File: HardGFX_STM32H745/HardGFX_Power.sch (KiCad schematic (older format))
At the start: 62 parts, among them J2 Conn_02x02_Odd_Even, J3 USB_C_Receptacle_USB2.0, U1 STM32H745BIT3, U2 ST1L05APU33R, U3 LD1117S18TR_SOT223, U4 LD1117S50TR_SOT223

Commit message: Add Info folder that contain data about reference design, datasheet component of references.
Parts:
- U1: value STM32H745BIT3 -> STM32H745BIT6; Digikey# (none) -> STM32H745BIT6-ND; MANUFACTURER (none) -> STMicroelectronics; Manf# (none) -> STM32H745BIT6
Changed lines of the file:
@@
 P 2650 1150
 F 0 "U1" H 3750 1537 60  0000 C CNN
-F 1 "STM32H745BIT3" H 3750 1431 60  0000 C CNN
+F 1 "STM32H745BIT6" H 3750 1431 60  0000 C CNN
 F 2 "STM32H745BIT3:STM32H745BIT3" H 3850 1390 60  0001 C CNN
 F 3 "https://www.st.com/resource/en/datasheet/stm32h745bi.pdf" H 2650 1150 60  0001 C CNN
+F 4 "STM32H745BIT6" H 2650 1150 50  0001 C CNN "Manf#"
+F 5 "STM32H745BIT6-ND" H 2650 1150 50  0001 C CNN "Digikey#"
+F 6 "STMicroelectronics" H 2650 1150 50  0001 C CNN "MANUFACTURER"
 	4    2650 1150
 	1    0    0    -1

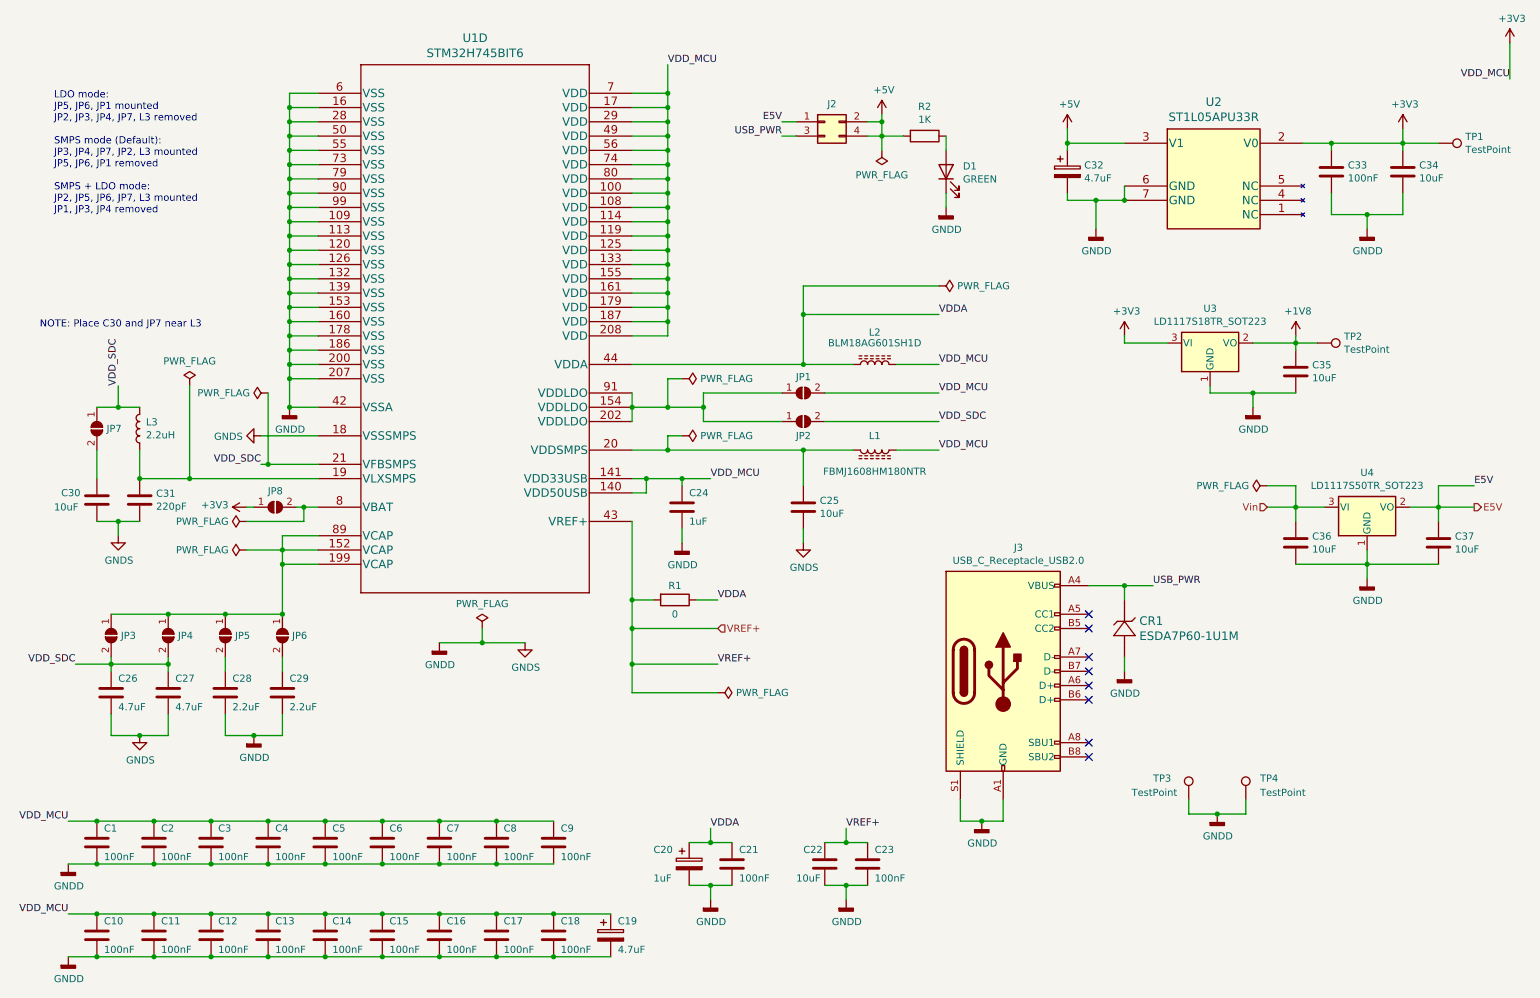
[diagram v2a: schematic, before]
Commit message: Filling field for do BOM with Kicost  and create proyect on IDE to start setting peripheral in MCU
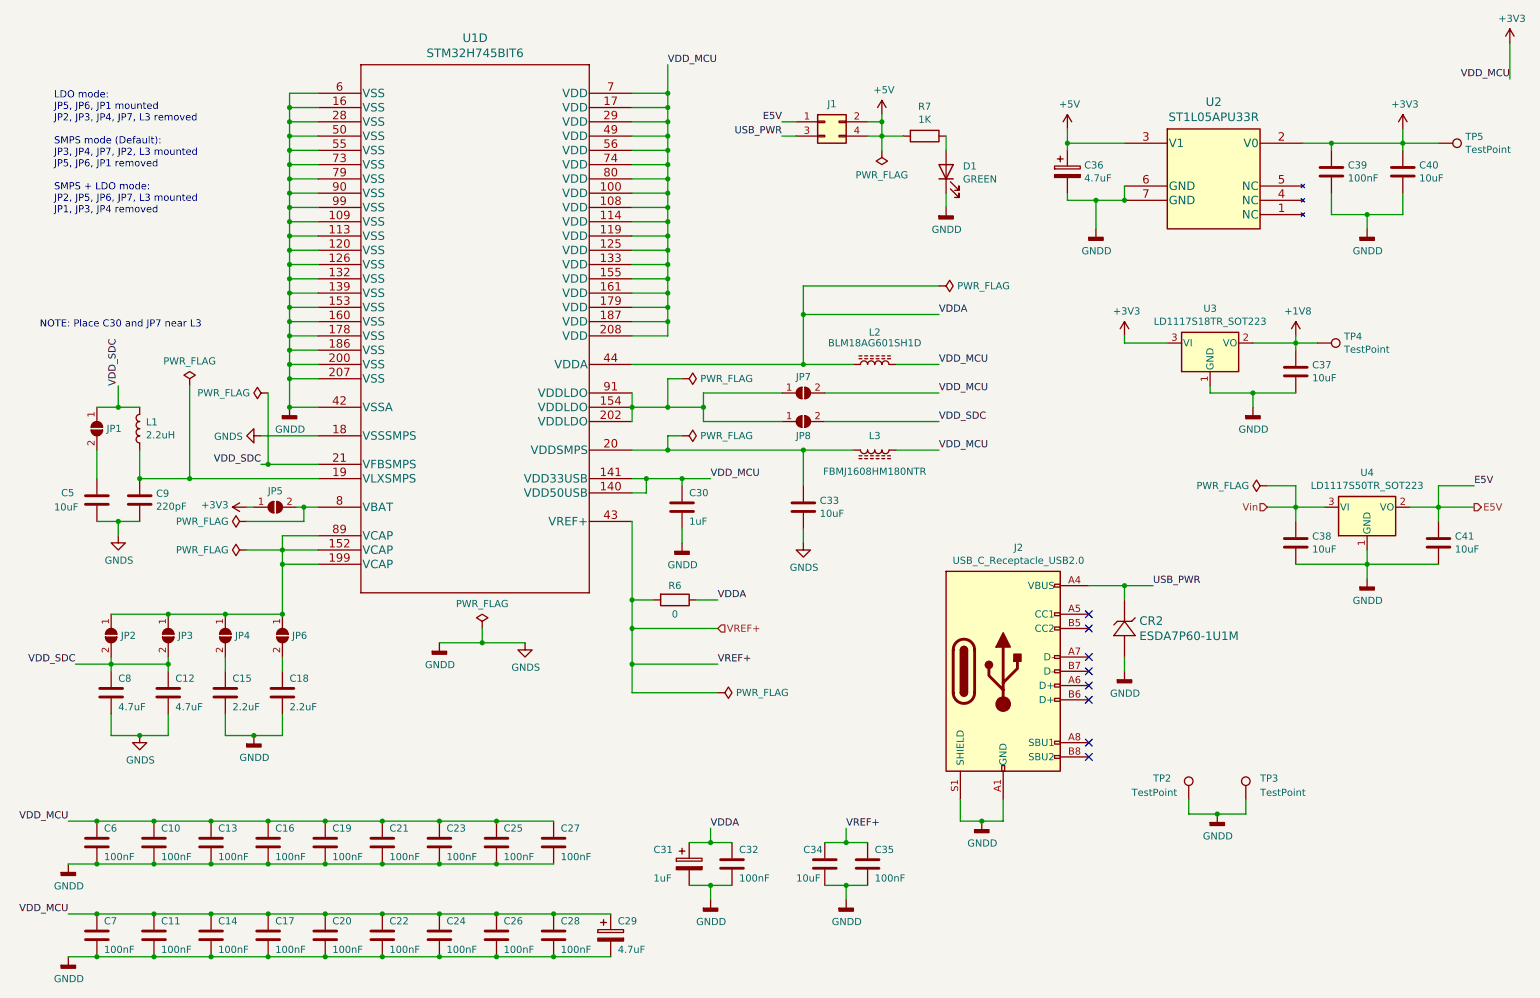
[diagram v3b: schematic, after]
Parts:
- CR2: renamed from CR1; Digikey# (none) -> 497-16253-1-ND; MANUFACTURER (none) -> STMicroelectronics; Manf# (none) -> ESDA7P60-1U1M; Mouser# (none) -> 511-ESDA7P60-1U1M
- D1: footprint LED_SMD:LED_0603_1608Metric -> LED_SMD:LED_1206_3216Metric; Digikey# (none) -> 732-5032-1-ND; MANUFACTURER (none) -> Wurth Elektronik; Manf# (none) -> 156120VS75000; Mouser# (none) -> 710-156120VS75000
- U1: Mouser# (none) -> 511-STM32H745BIT6
- U2: Digikey# (none) -> 497-8980-1-ND; MANUFACTURER (none) -> STMicroelectronics; Manf# (none) -> ST1L05APU33R; Mouser# (none) -> 511-ST1L05APU33R
- U3: Digikey# (none) -> 497-7308-1-ND; MANUFACTURER (none) -> STMicroelectronics; Manf# (none) -> LD1117S18TR; Mouser# (none) -> 511-LD1117S18-TR
- U4: Digikey# (none) -> 497-6447-1-ND; MANUFACTURER (none) -> STMicroelectronics; Manf# (none) -> LD1117S50TR; Mouser# (none) -> 511-LD1117S50
- renumbered C2 to C10, C27 to C12, C3 to C13, C12 to C14, C28 to C15, C4 to C16, C13 to C17, C29 to C18, C5 to C19, C14 to C20, C6 to C21, C15 to C22, C7 to C23, C16 to C24, C8 to C25, C17 to C26, C9 to C27, C18 to C28, C19 to C29, C24 to C30, C20 to C31, C21 to C32, C25 to C33, C22 to C34, C23 to C35, C32 to C36, C35 to C37, C36 to C38, C33 to C39, C34 to C40, C37 to C41, C30 to C5, C1 to C6, C10 to C7, C26 to C8, C31 to C9, J2 to J1, J3 to J2, JP7 to JP1, JP3 to JP2, JP4 to JP3, JP5 to JP4, JP8 to JP5, JP1 to JP7, JP2 to JP8, L3 to L1, L1 to L3, R1 to R6, R2 to R7, TP3 to TP2, TP4 to TP3, TP2 to TP4, TP1 to TP5

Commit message: I filled more component to Kicost script
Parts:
- J1: Digikey# (none) -> 75844-302-04LF-ND; MANUFACTURER (none) -> Amphenol FCI; Manf# (none) -> 75844-302-04LF; Mouser# (none) -> 649-75844-302-04LF
- J2: Digikey# (none) -> 12401610E4#2ACT-ND; MANUFACTURER (none) -> Amphenol Commercial Products; Manf# (none) -> 12401610E4#2A; Mouser# (none) -> 523-12401610E4#2A
- L1: Digikey# (none) -> 490-7786-1-ND; MANUFACTURER (none) -> Murata Electronics; Manf# (none) -> LQM2MPN2R2NG0L; Mouser# (none) -> 81-LQM2MPN2R2NG0L
- L2: Digikey# (none) -> 490-7811-1-ND; MANUFACTURER (none) -> Murata Electronics; Manf# (none) -> BLM18AG601SH1D; Mouser# (none) -> 81-BLM18AG601SH1D
- L3: Digikey# (none) -> 587-3251-1-ND; MANUFACTURER (none) -> Taiyo Yuden; Manf# (none) -> FBMJ1608HM180NTR; Mouser# (none) -> 963-FBMJ1608HM180NTR
- TP2, TP3, TP4, TP5: Digikey# (none) -> -; MANUFACTURER (none) -> -; Manf# (none) -> -; Mouser# (none) -> -
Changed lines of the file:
@@
 Sheet 2 8
 Title "Power"
-Date "2021-08-23"
+Date "2021-08-24"
 Rev "Rev. 1"
 Comp "HardGFX"
@@
 F 2 "Inductor_SMD:L_0603_1608Metric" H 6550 3650 50  0001 C CNN
 F 3 "https://ar.mouser.com/datasheet/2/396/TaiyoYuden_chipbeads01_e-1274227.pdf" H 6550 3650 50  0001 C CNN
+F 4 "587-3251-1-ND" H 6550 3650 50  0001 C CNN "Digikey#"
+F 5 "Taiyo Yuden" H 6550 3650 50  0001 C CNN "MANUFACTURER"
+F 6 "FBMJ1608HM180NTR" H 6550 3650 50  0001 C CNN "Manf#"
+F 7 "963-FBMJ1608HM180NTR" H 6550 3650 50  0001 C CNN "Mouser#"
 	1    6550 3650
 	0    1    1    0
@@
 F 1 "BLM18AG601SH1D" V 6700 3050 50  0000 C CNN
 F 2 "Inductor_SMD:L_0603_1608Metric" H 6550 3050 50  0001 C CNN
-F 3 "https://ar.mouser.com/datasheet/2/281/QNFA9101-1915702.pdf" H 6550 3050 50  0001 C CNN
+F 3 "https://www.murata.com/en-us/products/productdata/8796737273886/QNFA9101.pdf" H 6550 3050 50  0001 C CNN
+F 4 "490-7811-1-ND" H 6550 3050 50  0001 C CNN "Digikey#"
+F 5 "Murata Electronics" H 6550 3050 50  0001 C CNN "MANUFACTURER"
+F 6 "BLM18AG601SH1D" H 6550 3050 50  0001 C CNN "Manf#"
+F 7 "81-BLM18AG601SH1D" H 6550 3050 50  0001 C CNN "Mouser#"
 	1    6550 3050
 	0    -1   -1   0
@@
 F 1 "2.2uH" H 1356 3545 50  0000 R CNN
 F 2 "LQM2MPN2R2NG0L:INDC2016X100N" H 1400 3500 50  0001 C CNN
-F 3 "https://ar.mouser.com/datasheet/2/281/JELF243B-0022-1699512.pdf" H 1400 3500 50  0001 C CNN
+F 3 "https://search.murata.co.jp/Ceramy/image/img/P02/JELF243B-0022.pdf" H 1400 3500 50  0001 C CNN
+F 4 "490-7786-1-ND" H 1400 3500 50  0001 C CNN "Digikey#"
+F 5 "Murata Electronics" H 1400 3500 50  0001 C CNN "MANUFACTURER"
+F 6 "LQM2MPN2R2NG0L" H 1400 3500 50  0001 C CNN "Manf#"
+F 7 "81-LQM2MPN2R2NG0L" H 1400 3500 50  0001 C CNN "Mouser#"
 	1    1400 3500
 	-1   0    0    1
@@
 F 2 "TestPoint:TestPoint_Pad_D1.0mm" H 10700 1500 50  0001 C CNN
 F 3 "~" H 10700 1500 50  0001 C CNN
+F 4 "-" H 10500 1500 50  0001 C CNN "Digikey#"
+F 5 "-" H 10500 1500 50  0001 C CNN "MANUFACTURER"
+F 6 "-" H 10500 1500 50  0001 C CNN "Manf#"
+F 7 "-" H 10500 1500 50  0001 C CNN "Mouser#"
 	1    10500 1500
 	0    1    1    0
@@
 F 2 "TestPoint:TestPoint_Pad_D1.0mm" H 9850 2900 50  0001 C CNN
 F 3 "~" H 9850 2900 50  0001 C CNN
+F 4 "-" H 9650 2900 50  0001 C CNN "Digikey#"
+F 5 "-" H 9650 2900 50  0001 C CNN "MANUFACTURER"
+F 6 "-" H 9650 2900 50  0001 C CNN "Manf#"
+F 7 "-" H 9650 2900 50  0001 C CNN "Mouser#"
 	1    9650 2900
 	0    1    1    0
@@
 F 1 "Conn_02x02_Odd_Even" H 6250 1476 50  0001 C CNN
 F 2 "Connector_PinHeader_2.54mm:PinHeader_2x02_P2.54mm_Vertical" H 6200 1350 50  0001 C CNN
-F 3 "~" H 6200 1350 50  0001 C CNN
-F 4 "" H 6200 1350 50  0001 C CNN "MANUFACTURER"
-F 5 "" H 6200 1350 50  0001 C CNN "Manf#"
-F 6 "" H 6200 1350 50  0001 C CNN "Mouser#"
+F 3 "https://cdn.amphenol-icc.com/media/wysiwyg/files/drawing/75844.pdf" H 6200 1350 50  0001 C CNN
+F 4 "Amphenol FCI" H 6200 1350 50  0001 C CNN "MANUFACTURER"
+F 5 "75844-302-04LF" H 6200 1350 50  0001 C CNN "Manf#"
+F 6 "649-75844-302-04LF" H 6200 1350 50  0001 C CNN "Mouser#"
+F 7 "75844-302-04LF-ND" H 6200 1350 50  0001 C CNN "Digikey#"
 	1    6200 1350
 	1    0    0    -1
@@
 F 1 "USB_C_Receptacle_USB2.0" H 7557 5976 50  0000 C CNN
 F 2 "Connector_USB:USB_C_Receptacle_Amphenol_12401610E4-2A" H 7600 5200 50  0001 C CNN
-F 3 "" H 7600 5200 50  0001 C CNN
+F 3 "https://www.amphenol-icc.com/media/wysiwyg/files/drawing/12401610e4x2a.pdf" H 7600 5200 50  0001 C CNN
+F 4 "12401610E4#2ACT-ND" H 7450 5200 50  0001 C CNN "Digikey#"
+F 5 "Amphenol Commercial Products" H 7450 5200 50  0001 C CNN "MANUFACTURER"
+F 6 "12401610E4#2A" H 7450 5200 50  0001 C CNN "Manf#"
+F 7 "523-12401610E4#2A" H 7450 5200 50  0001 C CNN "Mouser#"
 	1    7450 5200
 	1    0    0    -1
@@
 F 2 "TestPoint:TestPoint_Pad_D1.0mm" H 8950 6100 50  0001 C CNN
 F 3 "~" H 8950 6100 50  0001 C CNN
+F 4 "-" H 8750 6100 50  0001 C CNN "Digikey#"
+F 5 "-" H 8750 6100 50  0001 C CNN "MANUFACTURER"
+F 6 "-" H 8750 6100 50  0001 C CNN "Manf#"
+F 7 "-" H 8750 6100 50  0001 C CNN "Mouser#"
 	1    8750 6100
 	1    0    0    -1
@@
 F 2 "TestPoint:TestPoint_Pad_D1.0mm" H 9350 6100 50  0001 C CNN
 F 3 "~" H 9350 6100 50  0001 C CNN
+F 4 "-" H 9150 6100 50  0001 C CNN "Digikey#"
+F 5 "-" H 9150 6100 50  0001 C CNN "MANUFACTURER"
+F 6 "-" H 9150 6100 50  0001 C CNN "Manf#"
+F 7 "-" H 9150 6100 50  0001 C CNN "Mouser#"
 	1    9150 6100
 	1    0    0    -1

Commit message: Almost I end to fill Kicost field on schematics.
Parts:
- C10, C11, C13, C14, C16, C17, C19, C20, C21, C22, C23, C24, C25, C26, C27, C28, C32, C35, C39, C6, C7: Digikey# (none) -> 311-1088-1-ND; MANUFACTURER (none) -> YAGEO; Manf# (none) -> CC0603KRX7R7BB104; Mouser# (none) -> 603-CC603KRX7R7BB104
- C12, C8: footprint Capacitor_SMD:C_0402_1005Metric -> (none); Digikey# (none) -> 490-12308-1-ND; MANUFACTURER (none) -> Murata Electronics; Manf# (none) -> GRT188R60J475ME01D; Mouser# (none) -> 81-GRT188R60J475ME1D
- C15, C18: Digikey# (none) -> 311-1451-1-ND; MANUFACTURER (none) -> YAGEO; Manf# (none) -> CC0603KRX5R6BB225; Mouser# (none) -> 603-CC603KRX5R6BB225
- C29, C36: Digikey# (none) -> 718-595D475X9016A2TCT-ND; MANUFACTURER (none) -> Vishay / Sprague; Manf# (none) -> 595D475X9016A2T; Mouser# (none) -> 74-595D475X9016A2T
- C30: Digikey# (none) -> 311-1444-1-ND; MANUFACTURER (none) -> YAGEO; Manf# (none) -> CC0603KRX5R7BB105; Mouser# (none) -> 603-CC603KRX5R7BB105
- C31: Digikey# (none) -> 718-595D105X9035A2TCT-ND; MANUFACTURER (none) -> Vishay / Sprague; Manf# (none) -> 595D105X9035A2T; Mouser# (none) -> 74-595D105X9035A2T
- C33: Digikey# (none) -> GRM155R60G106ME44J-ND; MANUFACTURER (none) -> Murata Electronics; Manf# (none) -> GRM155R60G106ME44J; Mouser# (none) -> 81-GRM155R60G106MEJ
- C34, C37, C38, C40, C41: Digikey# (none) -> 311-3503-1-ND; MANUFACTURER (none) -> YAGEO; Manf# (none) -> CC0805KRX5R8BB106; Mouser# (none) -> 603-CC0805KRX58BB106
- C5: Digikey# (none) -> 490-3896-1-ND; MANUFACTURER (none) -> Murata Electronics; Manf# (none) -> GRM188R60J106ME47D; Mouser# (none) -> 81-GRM188R60J106ME47
- C9: footprint Capacitor_SMD:C_0402_1005Metric -> (none); Digikey# (none) -> 311-1073-1-ND; MANUFACTURER (none) -> YAGEO; Manf# (none) -> CC0603JRNPO9BN221; Mouser# (none) -> 603-C0603JRNPO9BN221
- JP1, JP2, JP3, JP4, JP5, JP6, JP7, JP8: Digikey# (none) -> -; MANUFACTURER (none) -> -; Manf# (none) -> -; Mouser# (none) -> -
- R6: Digikey# (none) -> PMR03EZPJ000-ND; MANUFACTURER (none) -> ROHM Semiconductor; Manf# (none) -> PMR03EZPJ000; Mouser# (none) -> 755-PMR03EZPJ000
- R7: Digikey# (none) -> 311-1.00KHRCT-ND; MANUFACTURER (none) -> YAGEO; Manf# (none) -> RC0603FR-071KL; Mouser# (none) -> 603-RC0603FR-071KL

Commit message: Modified symbols field to use Kicost
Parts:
- C10, C11, C13, C14, C16, C17, C19, C20, C21, C22, C23, C24, C25, C26, C27, C28, C32, C35, C39, C6, C7: Manf# CC0603KRX7R7BB104 -> (none); manf# (none) -> CC0603KRX7R7BB104
- C12, C8: Manf# GRT188R60J475ME01D -> (none); manf# (none) -> GRT188R60J475ME01D
- C15, C18: Manf# CC0603KRX5R6BB225 -> (none); manf# (none) -> CC0603KRX5R6BB225
- C29, C36: Manf# 595D475X9016A2T -> (none); manf# (none) -> 595D475X9016A2T
- C30: Manf# CC0603KRX5R7BB105 -> (none); manf# (none) -> CC0603KRX5R7BB105
- C31: Manf# 595D105X9035A2T -> (none); manf# (none) -> 595D105X9035A2T
- C33: Manf# GRM155R60G106ME44J -> (none); manf# (none) -> GRM155R60G106ME44J
- C34, C37, C38, C40, C41: Manf# CC0805KRX5R8BB106 -> (none); manf# (none) -> CC0805KRX5R8BB106
- C5: Manf# GRM188R60J106ME47D -> (none); manf# (none) -> CC0603CRNPO9BN1R5
- C9: Manf# CC0603JRNPO9BN221 -> (none); manf# (none) -> CC0603JRNPO9BN221
- CR2: Manf# ESDA7P60-1U1M -> (none); manf# (none) -> ESDA7P60-1U1M
- D1: Manf# 156120VS75000 -> (none); manf# (none) -> 156120VS75000
- J1: Manf# 75844-302-04LF -> (none); manf# (none) -> 75844-302-04LF
- J2: Manf# 12401610E4#2A -> (none); manf# (none) -> 12401610E4#2A
- JP1, JP2, JP3, JP4, JP5, JP6, JP7, JP8, TP2, TP3, TP4, TP5: Manf# - -> (none); manf# (none) -> -
- L1: Manf# LQM2MPN2R2NG0L -> (none); manf# (none) -> LQM2MPN2R2NG0L
- L2: Manf# BLM18AG601SH1D -> (none); manf# (none) -> BLM18AG601SH1D
- L3: Manf# FBMJ1608HM180NTR -> (none); manf# (none) -> FBMJ1608HM180NTR
- R6: Manf# PMR03EZPJ000 -> (none); manf# (none) -> PMR03EZPJ000
- R7: Manf# RC0603FR-071KL -> (none); manf# (none) -> RC0603FR-071KL
- U1: Manf# STM32H745BIT6 -> (none); manf# (none) -> STM32H745BIT6
- U2: Manf# ST1L05APU33R -> (none); manf# (none) -> ST1L05APU33R
- U3: Manf# LD1117S18TR -> (none); manf# (none) -> LD1117S18TR
- U4: Manf# LD1117S50TR -> (none); manf# (none) -> LD1117S50TR
